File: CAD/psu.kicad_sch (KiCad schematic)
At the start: 36 parts, among them J1 220VAC, J2 Vout conn, J3 OLED Pins, J4 GND/-, Q1 tip35c, Q2 BD139, Q3 BC184C, Q4 BC547, SW1 Main, T1 220/24, U1 TL431LP, U2 LM317_TO-220, U3 DS18B20

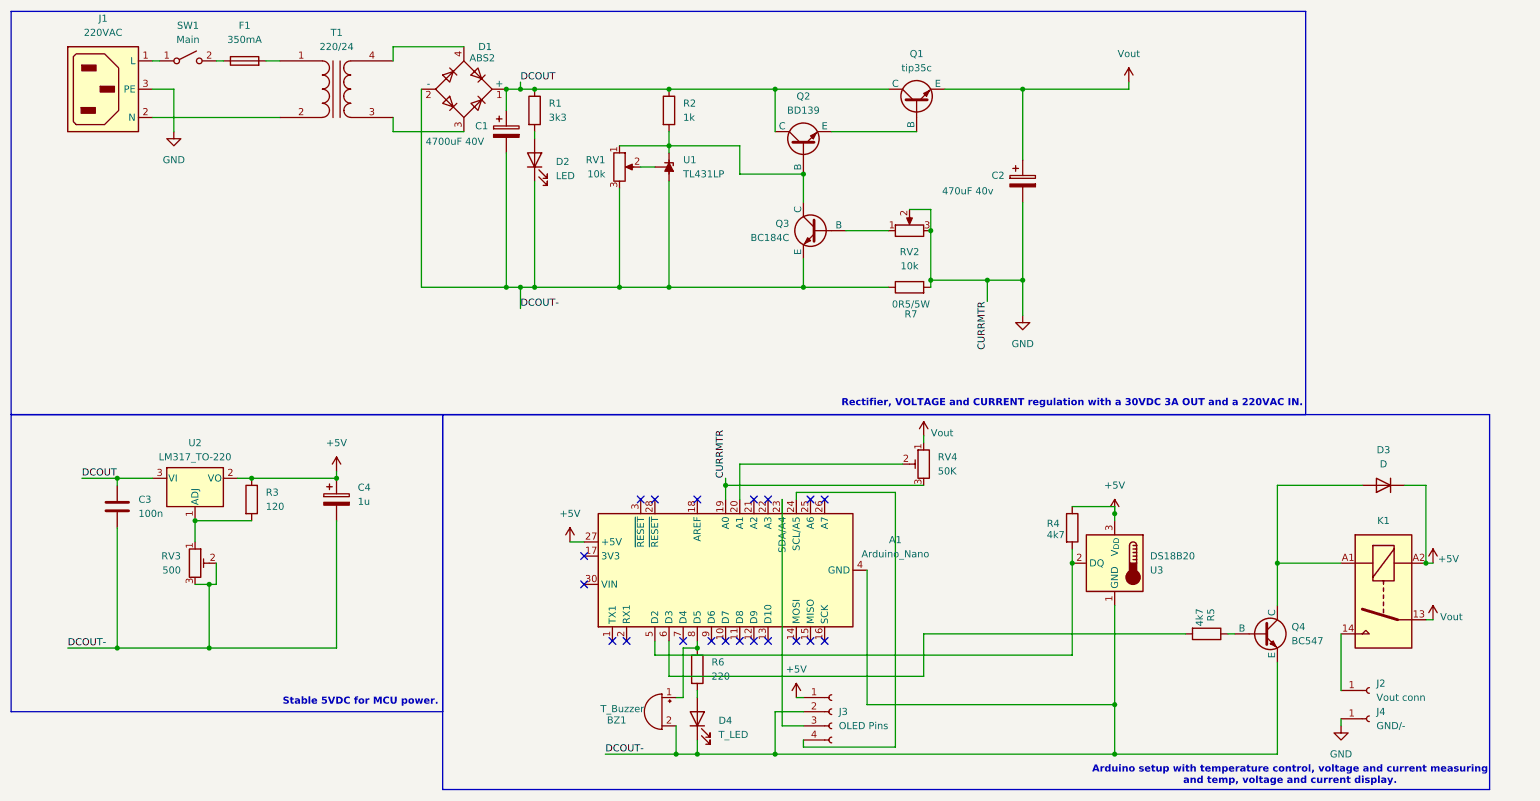
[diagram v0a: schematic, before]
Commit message: PCB and SCH finished and PDF for self manufacturing finished
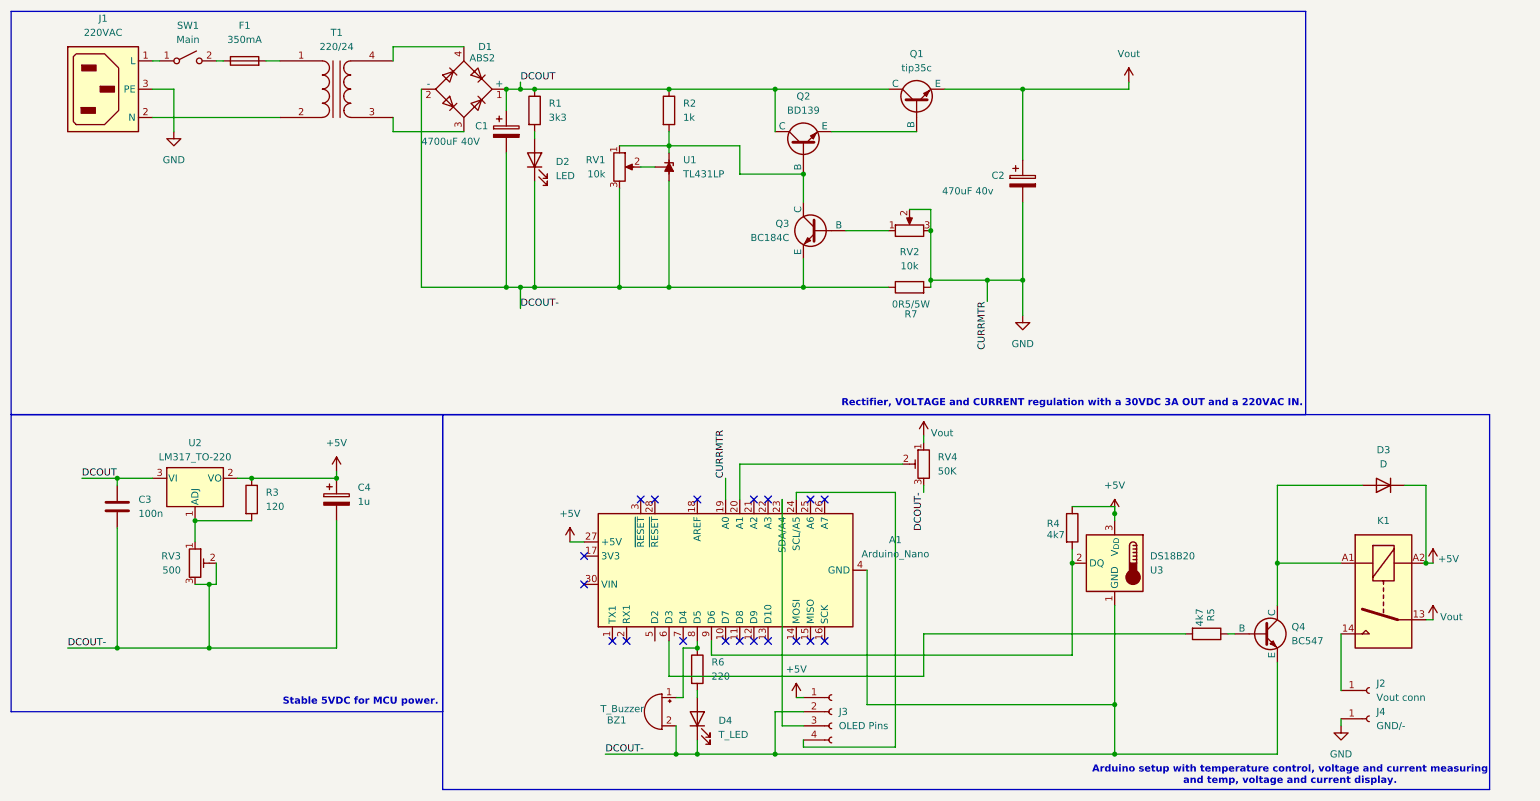
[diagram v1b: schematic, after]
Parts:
- T1: footprint Connector_PinHeader_2.54mm:PinHeader_1x02_P2.54mm_Vertical -> TerminalBlock_Altech:Altech_AK100_1x02_P5.00mm
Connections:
- net DCOUT-: now also RV4.3
- net GND: no longer RV4.3
- net at R4.2, U3.2 (DQ): now also A1.9 (D6); no longer A1.5 (D2)
- no-connect marks 20 -> 19
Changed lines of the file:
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@@
 	)
 	(junction
-		(at 140.97 97.79)
-		(diameter 0)
-		(color 0 0 0 0)
-	)
-	(junction
 		(at 132.08 146.05)
 		(diameter 0)
@@
 	)
 	(no_connect
-		(at 138.43 125.73)
-	)
-	(no_connect
 		(at 128.27 100.33)
 	)
@@
 	(wire
 		(pts
+			(xy 203.2 128.27) (xy 138.43 128.27)
+		)
+		(stroke
+			(width 0)
+			(type default)
+		)
+	)
+	(wire
+		(pts
+			(xy 176.53 97.79) (xy 176.53 99.06)
+		)
+		(stroke
+			(width 0)
+			(type default)
+		)
+	)
+	(wire
+		(pts
 			(xy 149.86 138.43) (xy 149.86 146.05)
 		)
@@
 	(wire
 		(pts
-			(xy 262.89 97.79) (xy 266.7 97.79)
+			(xy 138.43 125.73) (xy 138.43 128.27)
 		)
 		(stroke
@@
 	(wire
 		(pts
-			(xy 194.31 26.67) (xy 194.31 39.37)
+			(xy 262.89 97.79) (xy 266.7 97.79)
 		)
 		(stroke
@@
 	(wire
 		(pts
-			(xy 48.26 115.57) (xy 49.53 115.57)
+			(xy 194.31 26.67) (xy 194.31 39.37)
 		)
 		(stroke
@@
 	(wire
 		(pts
-			(xy 22.86 127) (xy 31.75 127)
+			(xy 48.26 115.57) (xy 49.53 115.57)
 		)
 		(stroke
@@
 	(wire
 		(pts
-			(xy 41.91 26.67) (xy 41.91 34.29)
+			(xy 22.86 127) (xy 31.75 127)
 		)
 		(stroke
@@
 	(wire
 		(pts
-			(xy 210.82 119.38) (xy 210.82 137.16)
+			(xy 41.91 26.67) (xy 41.91 34.29)
 		)
 		(stroke
@@
 	(wire
 		(pts
-			(xy 135.89 127) (xy 135.89 125.73)
+			(xy 210.82 119.38) (xy 210.82 137.16)
 		)
 		(stroke
@@
 	(wire
 		(pts
-			(xy 133.35 135.89) (xy 133.35 127)
+			(xy 135.89 127) (xy 135.89 125.73)
 		)
 		(stroke
@@
 	(wire
 		(pts
-			(xy 128.27 128.27) (xy 203.2 128.27)
+			(xy 133.35 135.89) (xy 133.35 127)
 		)
 		(stroke
@@
 	(wire
 		(pts
-			(xy 140.97 96.52) (xy 140.97 97.79)
+			(xy 140.97 96.52) (xy 140.97 100.33)
 		)
 		(stroke
@@
 	(wire
 		(pts
-			(xy 140.97 97.79) (xy 140.97 100.33)
-		)
-		(stroke
-			(width 0)
-			(type default)
-		)
-	)
-	(wire
-		(pts
 			(xy 149.86 26.67) (xy 149.86 34.29)
 		)
@@
 	(wire
 		(pts
-			(xy 128.27 125.73) (xy 128.27 128.27)
-		)
-		(stroke
-			(width 0)
-			(type default)
-		)
-	)
-	(wire
-		(pts
 			(xy 81.28 31.75) (xy 81.28 34.29)
 		)
@@
 	(wire
 		(pts
-			(xy 140.97 97.79) (xy 176.53 97.79)
-		)
-		(stroke
-			(width 0)
-			(type default)
-		)
-	)
-	(wire
-		(pts
 			(xy 231.14 124.46) (xy 232.41 124.46)
 		)
@@
 	)
 	(label "DCOUT-"
+		(at 176.53 99.06 270)
+		(effects
+			(font
+				(size 1.27 1.27)
+			)
+			(justify right bottom)
+		)
+	)
+	(label "DCOUT-"
 		(at 119.38 146.05 0)
 		(effects
@@
 		)
 		(property "Value" "4700uF 40V"
-			(at 87.122 36.068 0)
+			(at 86.36 36.068 0)
 			(show_name no)
 			(do_not_autoplace no)
@@
 			)
 		)
-		(property "Footprint" "Connector_PinHeader_2.54mm:PinHeader_1x02_P2.54mm_Vertical"
+		(property "Footprint" "TerminalBlock_Altech:Altech_AK100_1x02_P5.00mm"
 			(at 71.12 26.67 0)
 			(hide yes)
